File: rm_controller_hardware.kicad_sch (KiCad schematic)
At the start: 23 parts, among them J1 XT30PW-F_Horizontal, J10 XT30PW-F_Horizontal, J11 XT30PW-F_Horizontal, J12 XT30PW-F_Horizontal, J13 SM02B-GHS-TB, J14 SM02B-GHS-TB, J15 SM02B-GHS-TB, J16 SM02B-GHS-TB, J17 SM02B-GHS-TB, J18 SM02B-GHS-TB, J19 SM02B-GHS-TB, J2 XT30PW-F_Horizontal, J20 SM02B-GHS-TB, J21 RJ45, J22 RJ45, J3 XT60PW-M_Horizontal, J5 RJ45, J7 XT30PW-F_Horizontal, J8 XT30PW-F_Horizontal, J9 XT30PW-F_Horizontal, U2 BU33SD5WG-TR

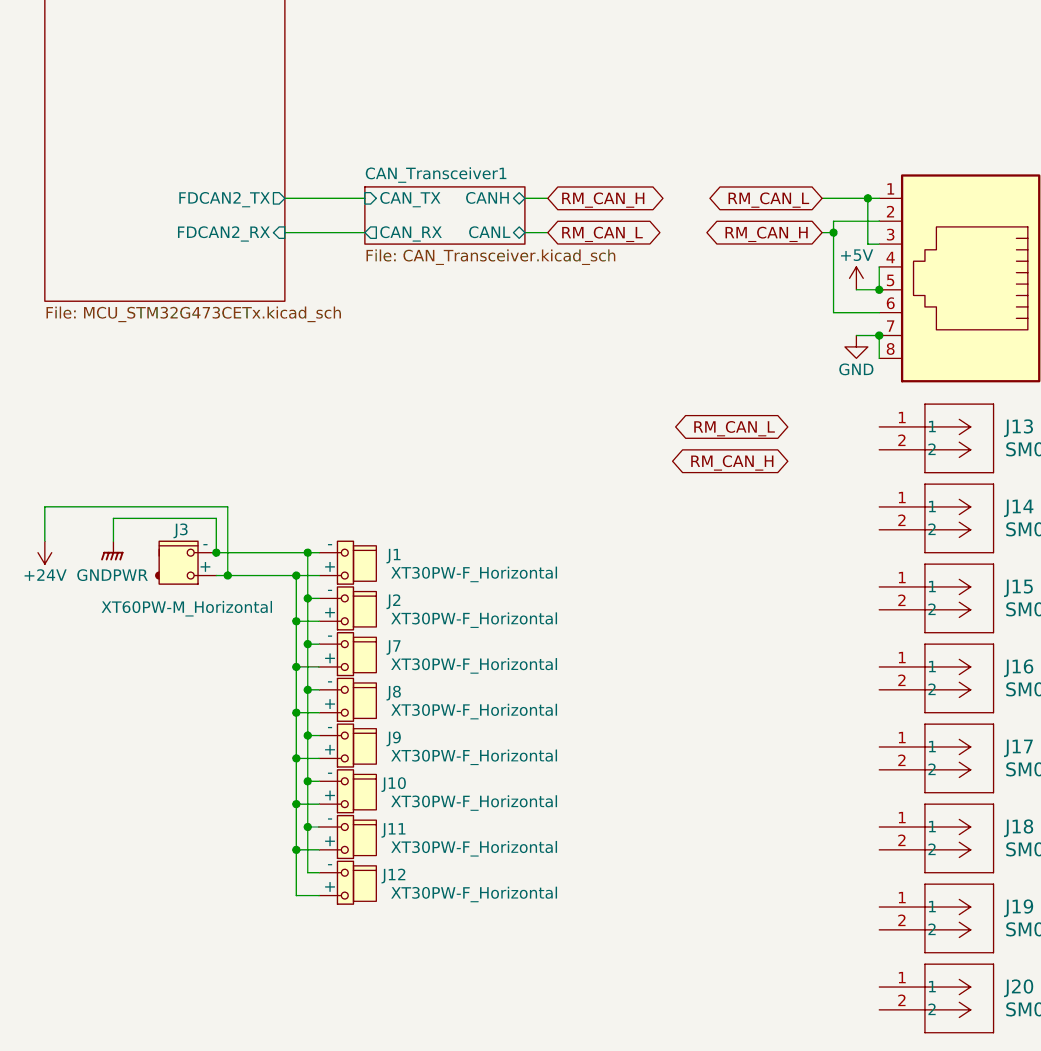
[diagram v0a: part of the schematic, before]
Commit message: apply .gitignore
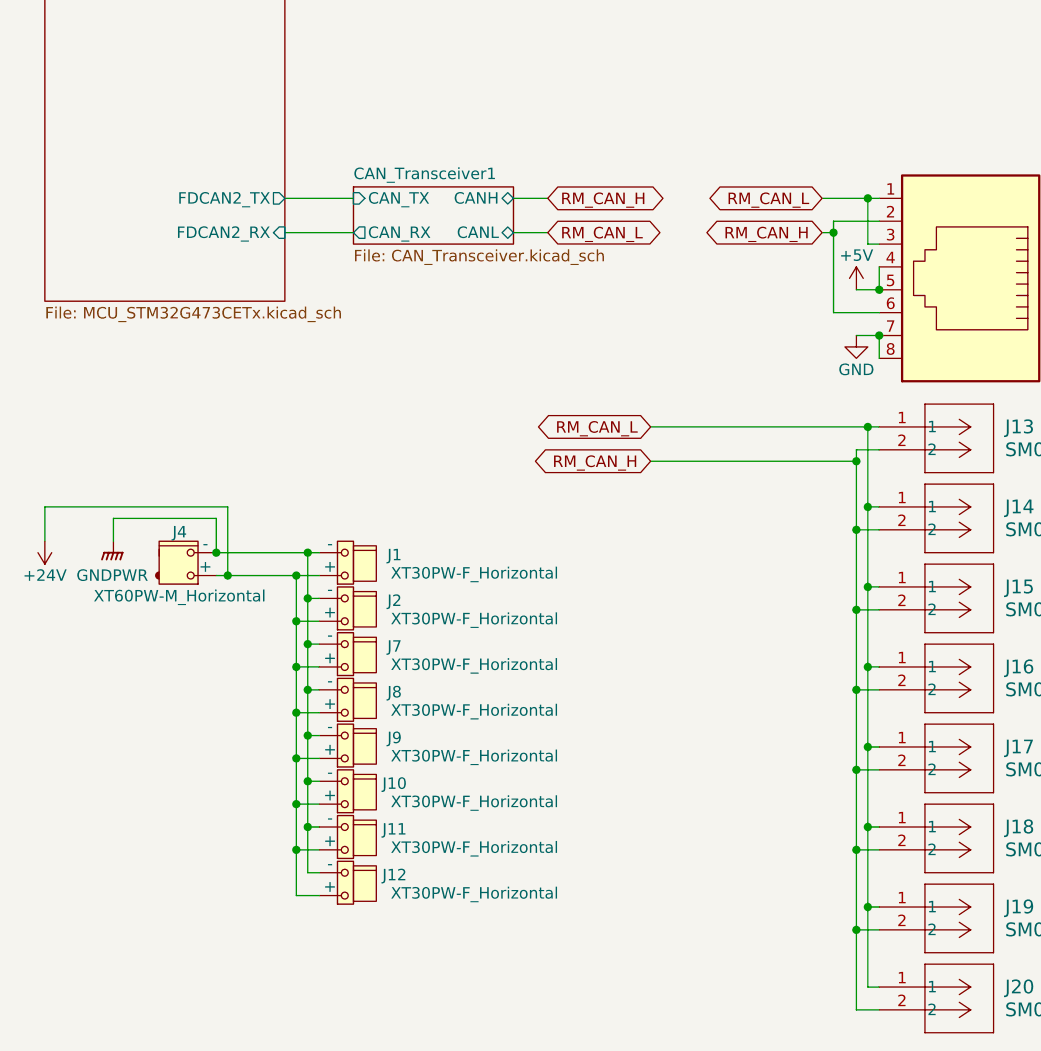
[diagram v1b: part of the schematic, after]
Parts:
- removed J3: XT60PW-M_Horizontal, Connector_AMASS:AMASS_XT60PW-M_1x02_P7.20mm_Horizontal, symbol y-robo:XT60PW-M_Horizontal
- added J4: XT60PW-M_Horizontal, Connector_AMASS:AMASS_XT60PW-M_1x02_P7.20mm_Horizontal, symbol y-robo:XT60PW-M_Horizontal
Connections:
- net +24V: now also J4.1 (+)
- net GNDPWR: now also J4.2 (-)
- net RM_CAN_H: now also J13.2, J14.2, J15.2, J16.2, J17.2, J18.2, J19.2, J20.2
- net RM_CAN_L: now also J13.1, J14.1, J15.1, J16.1, J17.1, J18.1, J19.1, J20.1

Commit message: ver1.00
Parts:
- removed J10, J11, J12, J2: XT30PW-F_Horizontal, Connector_AMASS:AMASS_XT30PW-F_1x02_P2.50mm_Horizontal, symbol y-robo:XT30PW-F_Horizontal
- removed J21: RJ45, symbol Connector:RJ45
- added J19: Conn_01x02_Pin, Connector_JST:JST_XH_B2B-XH-A_1x02_P2.50mm_Vertical, symbol Connector:Conn_01x02_Pin
- added J22: Conn_01x04_Pin, Connector_JST:JST_XH_S4B-XH-A_1x04_P2.50mm_Horizontal, symbol Connector:Conn_01x04_Pin
- added J3, J4, J5, J6: XT30PW-F_Horizontal, Connector_AMASS:AMASS_XT30PW-F_1x02_P2.50mm_Horizontal, symbol y-robo:XT30PW-F_Horizontal
- C1: renamed from C14; footprint (none) -> Capacitor_SMD:C_0603_1608Metric
- C2: renamed from C15; footprint (none) -> Capacitor_SMD:C_0603_1608Metric
- J18: renamed from J5; footprint (none) -> Connector_RJ:RJ45_Amphenol_54602-x08_Horizontal
- J20: renamed from J22; footprint (none) -> Connector_RJ:RJ45_Amphenol_54602-x08_Horizontal
- U1: renamed from U2; footprint SSOP5_ROM -> ul_BU33SD5WG-TR:SSOP5_ROM
- renumbered J4 to J1, J13 to J10, J14 to J11, J15 to J12, J16 to J13, J17 to J14, J18 to J15, J19 to J16, J20 to J17, J1 to J2
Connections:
- net +24V: now also J1.2 (+), J2.2 (+), J7.2 (+), J8.2 (+), J9.2 (+), J3.2 (+), J4.2 (+), J5.2 (+), J6.2 (+); no longer J1.1 (+), J2.1 (-), J7.1 (-), J8.1 (-), J9.1 (-)
- net +3.3V: now also J22.4 (Pin_4)
- net GND: now also J22.1 (Pin_1)
- net GNDPWR: now also J1.1 (-), J3.1 (-), J4.1 (-), J5.1 (-), J6.1 (-); no longer J1.2 (-)
- net RM_CAN_H: now also J19.1 (Pin_1)
- net RM_CAN_L: now also J19.2 (Pin_2)
- new net I2C_SDA: J22.3 (Pin_3)
- new net I2C_SDL: J22.2 (Pin_2)
